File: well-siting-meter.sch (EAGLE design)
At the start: 52 parts, among them J2 7805, K1 OJE-SH-105HM,000, T1 MOSFET-NCHANNELFQP30N06L, U1 LCD-16X2NOHOLES, U2 ARDUINO_PRO_MINI, U3 EC2, U4 EC2, U5 AD623, U6 AD629, U7 MAX1771

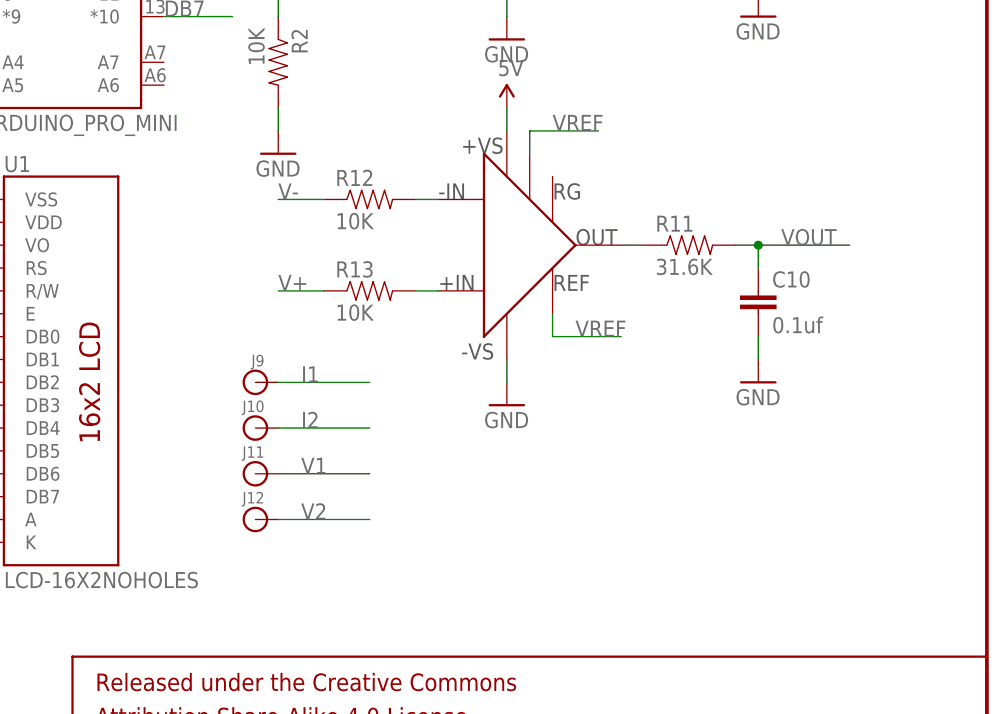
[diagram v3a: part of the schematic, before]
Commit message: rev B updates (AD629, fuse holder, power relay)
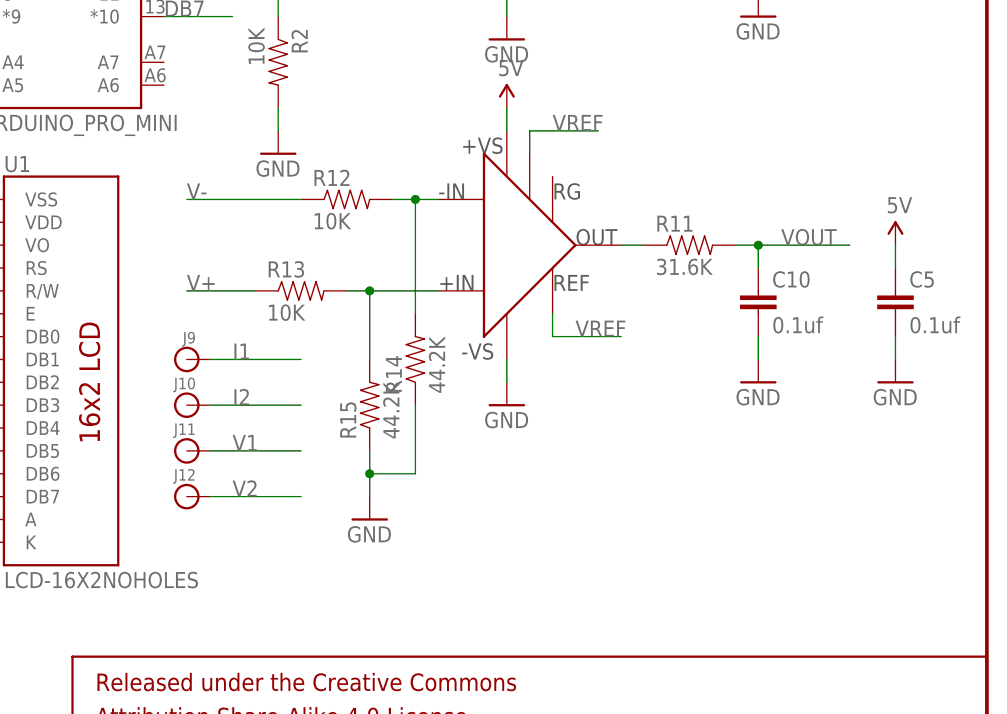
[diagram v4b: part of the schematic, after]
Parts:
- added C5: 0.1uf, SparkFun-Passives:CAPPTH1
- added R14, R15: 44.2K, SparkFun-Passives:RESISTORPTH-1/4W
- F1: PN (none) -> 36-3568-ND
- R12, R13: PN 2.05KXBK-ND -> 10.0KXBK-ND
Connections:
- net 5V: now also C5.1
- net GND: now also C5.2, R14.1, R15.1
- net N$13: now also R14.2
- net N$16: now also R15.2
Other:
- moved on the sheet: J10, J11, J12, J9, R12, R13
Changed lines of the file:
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@@
 <attribute name="PN" value="732-7163-ND"/>
 </part>
-<part name="F1" library="keystone" deviceset="3568" device=""/>
+<part name="F1" library="keystone" deviceset="3568" device="">
+<attribute name="PN" value="36-3568-ND"/>
+</part>
 <part name="SUPPLY1" library="SparkFun-Aesthetics" deviceset="V_BATT" device=""/>
 <part name="D4" library="SparkFun-DiscreteSemi" deviceset="DIODE" device="PTH">
@@
 </part>
 <part name="R12" library="SparkFun-Passives" deviceset="RESISTOR" device="PTH-1/4W" value="10K">
-<attribute name="PN" value="2.05KXBK-ND"/>
+<attribute name="PN" value="10.0KXBK-ND"/>
 </part>
 <part name="R13" library="SparkFun-Passives" deviceset="RESISTOR" device="PTH-1/4W" value="10K">
-<attribute name="PN" value="2.05KXBK-ND"/>
+<attribute name="PN" value="10.0KXBK-ND"/>
 </part>
+<part name="R14" library="SparkFun-Passives" deviceset="RESISTOR" device="PTH-1/4W" value="44.2K">
+<attribute name="PN" value="44.2KXBK-ND"/>
+</part>
+<part name="R15" library="SparkFun-Passives" deviceset="RESISTOR" device="PTH-1/4W" value="44.2K">
+<attribute name="PN" value="44.2KXBK-ND"/>
+</part>
+<part name="GND17" library="SparkFun-Aesthetics" deviceset="GND" device=""/>
+<part name="C5" library="SparkFun-Passives" deviceset="CAP" device="PTH1" value="0.1uf">
+<attribute name="PN" value="BC2665CT-ND"/>
+</part>
+<part name="SUPPLY12" library="SparkFun-Aesthetics" deviceset="5V" device=""/>
+<part name="GND18" library="SparkFun-Aesthetics" deviceset="GND" device=""/>
 </parts>
 <sheets>
@@
 <instance part="GND11" gate="1" x="134.62" y="43.18"/>
 <instance part="SUPPLY11" gate="G$1" x="132.08" y="88.9"/>
-<instance part="J12" gate="G$1" x="167.64" y="50.8" rot="MR0">
-<attribute name="PN" x="167.64" y="50.8" size="1.778" layer="96" rot="MR0" display="off"/>
+<instance part="J12" gate="G$1" x="160.02" y="53.34" rot="MR0">
+<attribute name="PN" x="160.02" y="53.34" size="1.778" layer="96" rot="MR0" display="off"/>
 </instance>
 <instance part="J7" gate="G$1" x="30.48" y="119.38" rot="MR0">
@@
 <attribute name="PN" x="30.48" y="114.3" size="1.778" layer="96" rot="MR0" display="off"/>
 </instance>
-<instance part="J9" gate="G$1" x="167.64" y="66.04" rot="MR0">
-<attribute name="PN" x="167.64" y="66.04" size="1.778" layer="96" rot="MR0" display="off"/>
-</instance>
-<instance part="J10" gate="G$1" x="167.64" y="60.96" rot="MR0">
-<attribute name="PN" x="167.64" y="60.96" size="1.778" layer="96" rot="MR0" display="off"/>
-</instance>
-<instance part="J11" gate="G$1" x="167.64" y="55.88" rot="MR0">
-<attribute name="PN" x="167.64" y="55.88" size="1.778" layer="96" rot="MR0" display="off"/>
+<instance part="J9" gate="G$1" x="160.02" y="68.58" rot="MR0">
+<attribute name="PN" x="160.02" y="68.58" size="1.778" layer="96" rot="MR0" display="off"/>
+</instance>
+<instance part="J10" gate="G$1" x="160.02" y="63.5" rot="MR0">
+<attribute name="PN" x="160.02" y="63.5" size="1.778" layer="96" rot="MR0" display="off"/>
+</instance>
+<instance part="J11" gate="G$1" x="160.02" y="58.42" rot="MR0">
+<attribute name="PN" x="160.02" y="58.42" size="1.778" layer="96" rot="MR0" display="off"/>
 </instance>
 <instance part="GND13" gate="1" x="93.98" y="139.7"/>
@@
 <attribute name="PN" x="73.66" y="83.82" size="1.778" layer="96" rot="R90" display="off"/>
 </instance>
-<instance part="F1" gate="G$1" x="48.26" y="119.38"/>
+<instance part="F1" gate="G$1" x="48.26" y="119.38">
+<attribute name="PN" x="48.26" y="119.38" size="1.778" layer="96" display="off"/>
+</instance>
 <instance part="SUPPLY1" gate="G$1" x="93.98" y="121.92"/>
 <instance part="D4" gate="G$1" x="55.88" y="111.76" rot="MR90">
@@
 <attribute name="PN" x="60.96" y="119.38" size="1.778" layer="96" display="off"/>
 </instance>
-<instance part="R12" gate="G$1" x="180.34" y="86.36">
-<attribute name="PN" x="180.34" y="86.36" size="1.778" layer="96" display="off"/>
-</instance>
-<instance part="R13" gate="G$1" x="180.34" y="76.2">
-<attribute name="PN" x="180.34" y="76.2" size="1.778" layer="96" display="off"/>
-</instance>
+<instance part="R12" gate="G$1" x="177.8" y="86.36">
+<attribute name="PN" x="177.8" y="86.36" size="1.778" layer="96" display="off"/>
+</instance>
+<instance part="R13" gate="G$1" x="172.72" y="76.2">
+<attribute name="PN" x="172.72" y="76.2" size="1.778" layer="96" display="off"/>
+</instance>
+<instance part="R14" gate="G$1" x="185.42" y="68.58" rot="R90">
+<attribute name="PN" x="185.42" y="68.58" size="1.778" layer="96" rot="R90" display="off"/>
+</instance>
+<instance part="R15" gate="G$1" x="180.34" y="63.5" rot="R90">
+<attribute name="PN" x="180.34" y="63.5" size="1.778" layer="96" rot="R90" display="off"/>
+</instance>
+<instance part="GND17" gate="1" x="180.34" y="50.8"/>
+<instance part="C5" gate="G$1" x="238.76" y="73.66">
+<attribute name="PN" x="238.76" y="73.66" size="1.778" layer="96" display="off"/>
+</instance>
+<instance part="SUPPLY12" gate="G$1" x="238.76" y="81.28"/>
+<instance part="GND18" gate="1" x="238.76" y="66.04"/>
 </instances>
 <busses>
@@
 <wire x1="68.58" y1="93.98" x2="68.58" y2="91.44" width="0.1524" layer="91"/>
 </segment>
+<segment>
+<pinref part="R15" gate="G$1" pin="1"/>
+<pinref part="GND17" gate="1" pin="GND"/>
+<wire x1="180.34" y1="58.42" x2="180.34" y2="55.88" width="0.1524" layer="91"/>
+<junction x="180.34" y="55.88"/>
+<wire x1="180.34" y1="55.88" x2="180.34" y2="53.34" width="0.1524" layer="91"/>
+<pinref part="R14" gate="G$1" pin="1"/>
+<wire x1="185.42" y1="63.5" x2="185.42" y2="55.88" width="0.1524" layer="91"/>
+<wire x1="185.42" y1="55.88" x2="180.34" y2="55.88" width="0.1524" layer="91"/>
+</segment>
+<segment>
+<pinref part="C5" gate="G$1" pin="2"/>
+<pinref part="GND18" gate="1" pin="GND"/>
+<wire x1="238.76" y1="71.12" x2="238.76" y2="68.58" width="0.1524" layer="91"/>
+</segment>
 </net>
 <net name="5V" class="0">
@@
 <wire x1="132.08" y1="50.8" x2="137.16" y2="50.8" width="0.1524" layer="91"/>
 <junction x="132.08" y="83.82"/>
+</segment>
+<segment>
+<pinref part="SUPPLY12" gate="G$1" pin="5V"/>
+<pinref part="C5" gate="G$1" pin="1"/>
+<wire x1="238.76" y1="81.28" x2="238.76" y2="78.74" width="0.1524" layer="91"/>
 </segment>
 </net>
@@
 <segment>
 <pinref part="J9" gate="G$1" pin="1"/>
-<wire x1="170.18" y1="66.04" x2="180.34" y2="66.04" width="0.1524" layer="91"/>
-<label x="172.72" y="66.04" size="1.778" layer="95"/>
+<wire x1="162.56" y1="68.58" x2="172.72" y2="68.58" width="0.1524" layer="91"/>
+<label x="165.1" y="68.58" size="1.778" layer="95"/>
 </segment>
 </net>
@@
 <segment>
 <pinref part="J10" gate="G$1" pin="1"/>
-<wire x1="170.18" y1="60.96" x2="180.34" y2="60.96" width="0.1524" layer="91"/>
-<label x="172.72" y="60.96" size="1.778" layer="95"/>
+<wire x1="162.56" y1="63.5" x2="172.72" y2="63.5" width="0.1524" layer="91"/>
+<label x="165.1" y="63.5" size="1.778" layer="95"/>
 </segment>
 </net>
@@
 <segment>
 <pinref part="R13" gate="G$1" pin="1"/>
-<wire x1="175.26" y1="76.2" x2="170.18" y2="76.2" width="0.1524" layer="91"/>
-<label x="170.18" y="76.2" size="1.778" layer="95"/>
+<wire x1="167.64" y1="76.2" x2="160.02" y2="76.2" width="0.1524" layer="91"/>
+<label x="160.02" y="76.2" size="1.778" layer="95"/>
 </segment>
 </net>
@@
 <segment>
 <pinref part="R12" gate="G$1" pin="1"/>
-<wire x1="175.26" y1="86.36" x2="170.18" y2="86.36" width="0.1524" layer="91"/>
-<label x="170.18" y="86.36" size="1.778" layer="95"/>
+<wire x1="172.72" y1="86.36" x2="160.02" y2="86.36" width="0.1524" layer="91"/>
+<label x="160.02" y="86.36" size="1.778" layer="95"/>
 </segment>
 </net>
@@
 <segment>
 <pinref part="J12" gate="G$1" pin="1"/>
-<wire x1="170.18" y1="50.8" x2="180.34" y2="50.8" width="0.1524" layer="91"/>
-<label x="172.72" y="50.8" size="1.778" layer="95"/>
+<wire x1="162.56" y1="53.34" x2="172.72" y2="53.34" width="0.1524" layer="91"/>
+<label x="165.1" y="53.34" size="1.778" layer="95"/>
 </segment>
 </net>
@@
 <segment>
 <pinref part="J11" gate="G$1" pin="1"/>
-<wire x1="170.18" y1="55.88" x2="180.34" y2="55.88" width="0.1524" layer="91"/>
-<label x="172.72" y="55.88" size="1.778" layer="95"/>
+<wire x1="162.56" y1="58.42" x2="172.72" y2="58.42" width="0.1524" layer="91"/>
+<label x="165.1" y="58.42" size="1.778" layer="95"/>
 </segment>
 </net>
@@
 <pinref part="R12" gate="G$1" pin="2"/>
 <pinref part="U6" gate="G$1" pin="-IN"/>
+<wire x1="182.88" y1="86.36" x2="185.42" y2="86.36" width="0.1524" layer="91"/>
+<junction x="185.42" y="86.36"/>
 <wire x1="185.42" y1="86.36" x2="187.96" y2="86.36" width="0.1524" layer="91"/>
+<pinref part="R14" gate="G$1" pin="2"/>
+<wire x1="185.42" y1="73.66" x2="185.42" y2="86.36" width="0.1524" layer="91"/>
 </segment>
 </net>
@@
 <pinref part="R13" gate="G$1" pin="2"/>
 <pinref part="U6" gate="G$1" pin="+IN"/>
-<wire x1="185.42" y1="76.2" x2="187.96" y2="76.2" width="0.1524" layer="91"/>
-</segment>
-</net>
+<wire x1="177.8" y1="76.2" x2="180.34" y2="76.2" width="0.1524" layer="91"/>
+<junction x="180.34" y="76.2"/>
+<wire x1="180.34" y1="76.2" x2="187.96" y2="76.2" width="0.1524" layer="91"/>
+<pinref part="R15" gate="G$1" pin="2"/>
+<wire x1="180.34" y1="76.2" x2="180.34" y2="68.58" width="0.1524" layer="91"/>
+</segment>
+</net>
